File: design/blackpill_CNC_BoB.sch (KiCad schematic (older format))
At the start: 291 parts, among them J101 ALimIN, J102 ZLimIN, J103 YLimIN, J104 XLimIN, J105 CS_IN, J106 FH_IN, J107 DoorIN, J108 ResetIN, J109 ProbeIN, J110 12V Power in, J111 AuxEncIn, J112 5V Power out, J113 ADC_in_1, J114 ADC_in_2, J115 stepDriverLim, J116 Reset, J117 UART1, J118 I2C, J119 SpindleVFD, J120 Spindle/Coolant, J121 Spindle, J122 Coolant, J123 AuxOut, J124 XStepDrv, J125 YStepDrv, J126 ZStepDrv, J127 AStepDrv, U101 TLP290-4, U102 TLP290-4, U103 TLP290-4, U104 74LVC2G17, U105 LD1117S50TR_SOT223, U106 LM358, U107 TLV9001, U108 TLV9001, U109 YAAJ_WeAct_BlackPill_Part_Like, U110 TLV9001, U111 TLV9001, U112 74HCT541, U113 74HCT541, U114 74HCT541, U115 ULN2003A, U116 ULN2003A, U117 ULN2003A

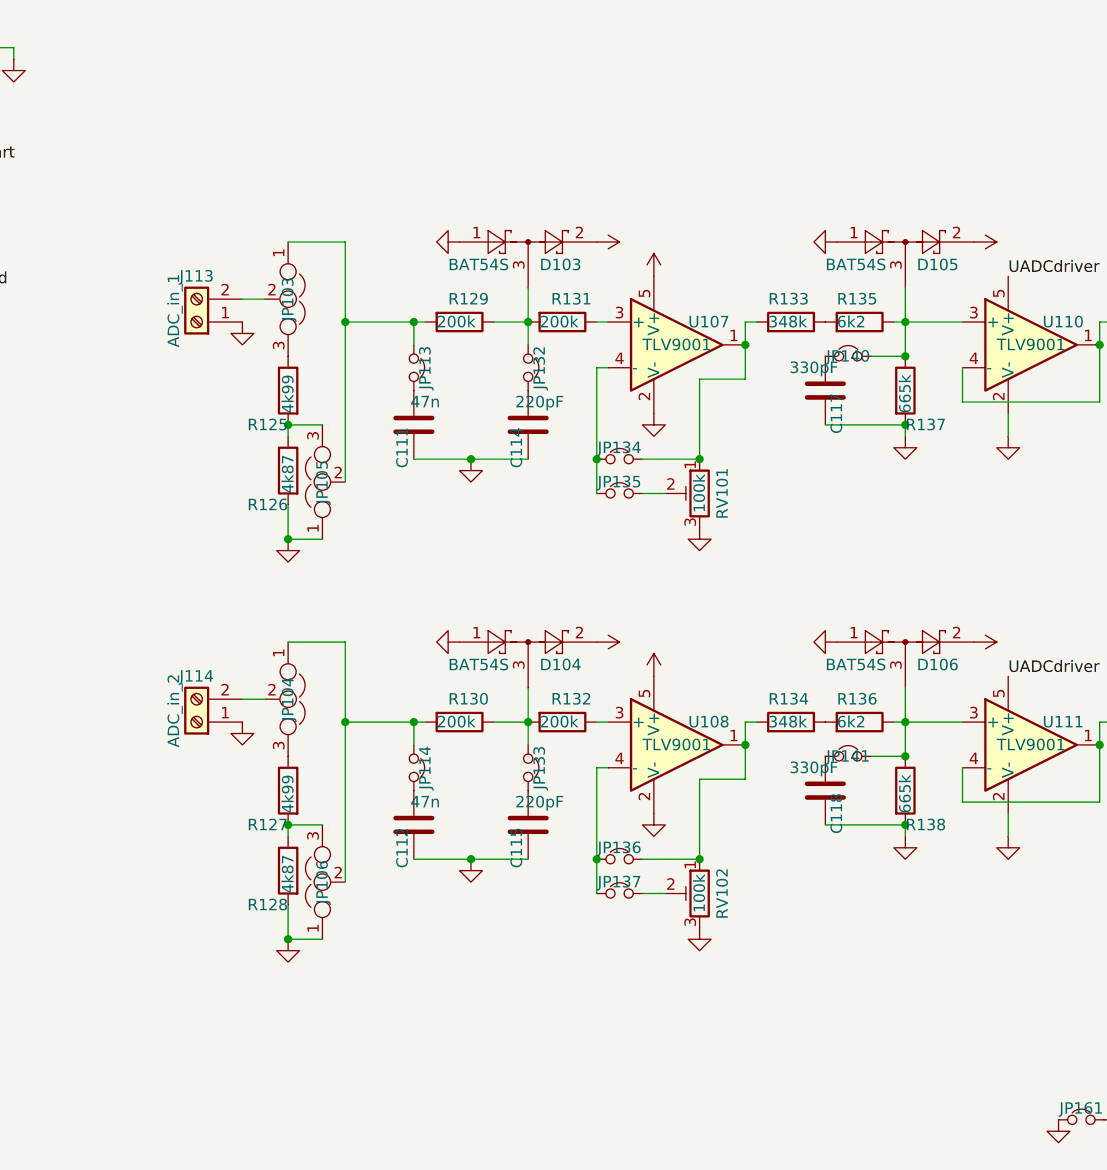
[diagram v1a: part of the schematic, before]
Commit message: JLBPCB tuned resistors
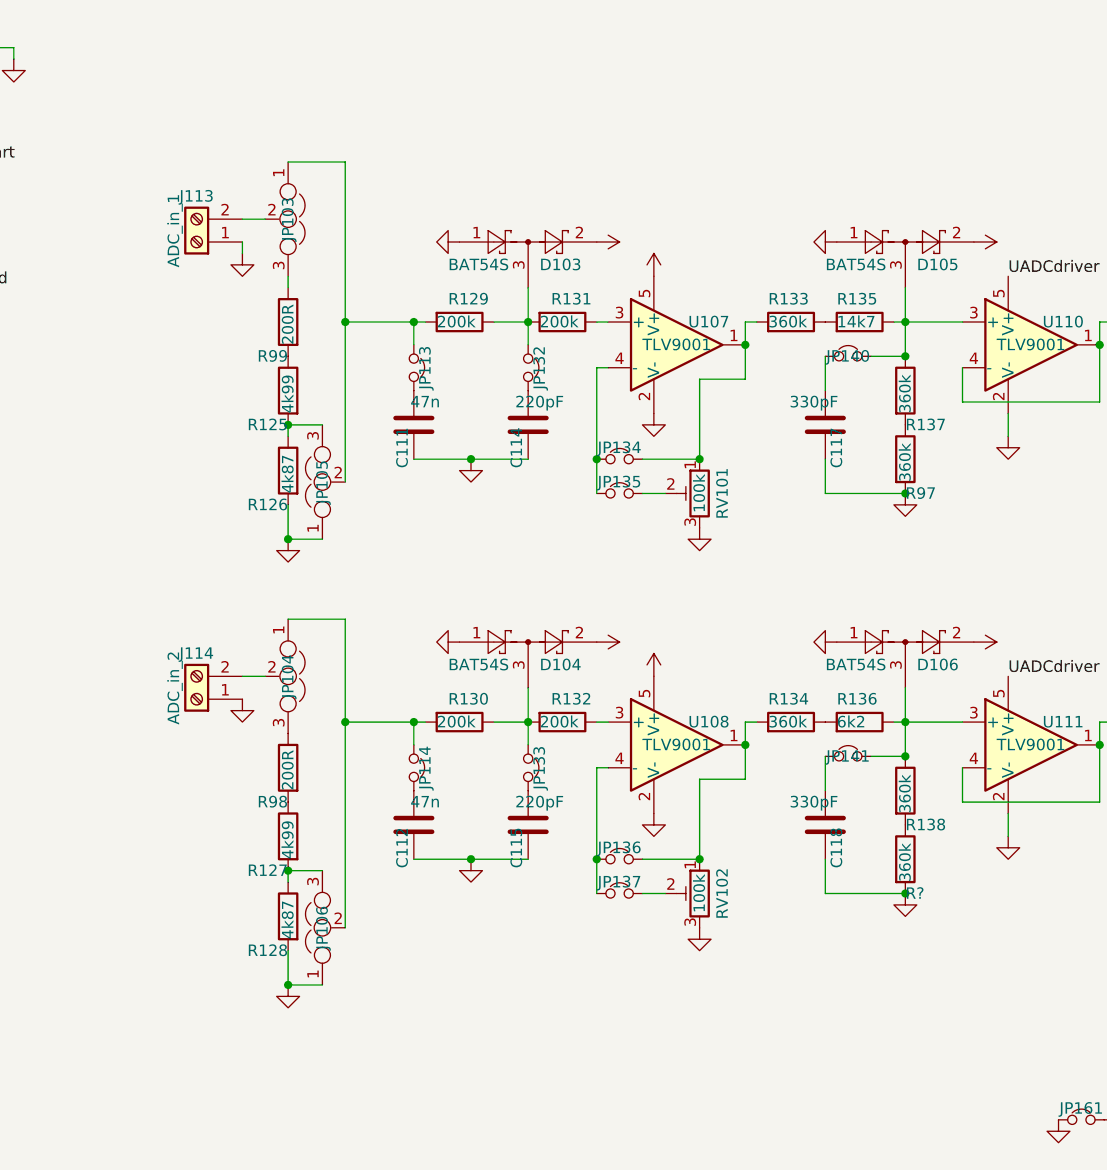
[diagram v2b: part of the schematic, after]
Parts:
- added R97, R?: 360k, symbol Device:R
- added R98, R99: 200R, symbol Device:R
- R133, R134: value 348k -> 360k
- R135: value 6k2 -> 14k7
- R137, R138: value 665k -> 360k
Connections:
- net GND: now also R97.2, R?.2; no longer R137.2, R138.2
- net at JP103.3: now also R99.1; no longer R125.1
- net at JP104.3: now also R98.1; no longer R127.1
- new net: R125.1, R99.2
- new net: R127.1, R98.2
- new net: R137.2, R97.1
- new net: R138.2, R?.1
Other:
- moved on the sheet: C117, C118, J113, J114, JP103, JP104, JP106, R127, R128
